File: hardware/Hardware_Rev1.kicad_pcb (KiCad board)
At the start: 2 copper layers, 147.3 x 100.3 mm, 163 parts, among them J1 RJ45_LED_Shielded, J2 6P6C, Q1 BSS138, Q10 AO3401A, Q11 AO3401A, Q12 AO3401A, Q13 BSS138, Q14 BSS138, Q15 BSS138, Q16 AO3401A, Q17 AO3401A, Q18 AO3401A, Q19 BSS138, Q2 BSS138, Q20 BSS138, Q21 BSS138, Q22 AO3401A, Q23 AO3401A, Q24 AO3401A, Q3 BSS138, Q4 AO3401A, Q5 AO3401A, Q6 AO3401A, Q7 BSS138, Q8 BSS138, Q9 BSS138, U1 OKI, U2 Teensy4.1_DEV-16771

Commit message: Fixed mosfet circuits
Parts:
- turned Q10 to -90 degrees
- turned Q11 to -90 degrees
- turned Q12 to -90 degrees
- turned Q16 to -90 degrees
- turned Q17 to -90 degrees
- turned Q18 to -90 degrees
- turned Q22 to -90 degrees
- turned Q23 to -90 degrees
- turned Q24 to -90 degrees
- turned Q4 to -90 degrees
- turned Q5 to -90 degrees
- turned Q6 to -90 degrees
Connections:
- Q10 pad 2: Net-(Conn8-Pad1) -> +12V
- Q10 pad 3: +12V -> Net-(Conn8-Pad1)
- Q11 pad 2: Net-(Conn10-Pad1) -> +12V
- Q11 pad 3: +12V -> Net-(Conn10-Pad1)
- Q12 pad 2: Net-(Conn12-Pad1) -> +12V
- Q12 pad 3: +12V -> Net-(Conn12-Pad1)
- Q16 pad 2: Net-(Conn14-Pad1) -> +12V
- Q16 pad 3: +12V -> Net-(Conn14-Pad1)
- Q17 pad 2: Net-(Conn16-Pad1) -> +12V
- Q17 pad 3: +12V -> Net-(Conn16-Pad1)
- Q18 pad 2: Net-(Conn18-Pad1) -> +12V
- Q18 pad 3: +12V -> Net-(Conn18-Pad1)
- Q22 pad 2: Net-(Conn20-Pad1) -> +12V
- Q22 pad 3: +12V -> Net-(Conn20-Pad1)
- Q23 pad 2: Net-(Conn22-Pad1) -> +12V
- Q23 pad 3: +12V -> Net-(Conn22-Pad1)
- Q24 pad 2: Net-(Conn24-Pad1) -> +12V
- Q24 pad 3: +12V -> Net-(Conn24-Pad1)
- Q4 pad 2: Net-(Conn2-Pad1) -> +12V
- Q4 pad 3: +12V -> Net-(Conn2-Pad1)
- Q5 pad 2: Net-(Conn4-Pad1) -> +12V
- Q5 pad 3: +12V -> Net-(Conn4-Pad1)
- Q6 pad 2: Net-(Conn6-Pad1) -> +12V
- Q6 pad 3: +12V -> Net-(Conn6-Pad1)
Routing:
- net +12V: track 38.9 -> 27.5 mm
- net Net-(Q5-Pad1): track 3.82 -> 12.7 mm, vias 0 -> 2
- net Net-(Q22-Pad1): track 3.76 -> 12.6 mm, vias 0 -> 2
- net Net-(Q16-Pad1): track 3.76 -> 12.6 mm, vias 0 -> 2
- net Net-(Q6-Pad1): track 3.76 -> 12.6 mm, vias 0 -> 2
- net Net-(Q18-Pad1): track 3.76 -> 12.6 mm, vias 0 -> 2
- net Net-(Q12-Pad1): track 3.76 -> 12.6 mm, vias 0 -> 2
- net Net-(Q10-Pad1): track 3.76 -> 12.6 mm, vias 0 -> 2
- net Net-(Q23-Pad1): track 3.78 -> 12.5 mm, vias 0 -> 2
- net Net-(Q24-Pad1): track 3.79 -> 12.5 mm, vias 0 -> 2
- net Net-(Q11-Pad1): track 3.91 -> 12.5 mm, vias 0 -> 2
- net Net-(Q4-Pad1): track 3.77 -> 12.3 mm, vias 0 -> 2
- net Net-(Q17-Pad1): track 3.78 -> 12.3 mm, vias 0 -> 2
- net Heater4: track 35.1 -> 43.3 mm
- net Heater2: track 51.6 -> 59.8 mm
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
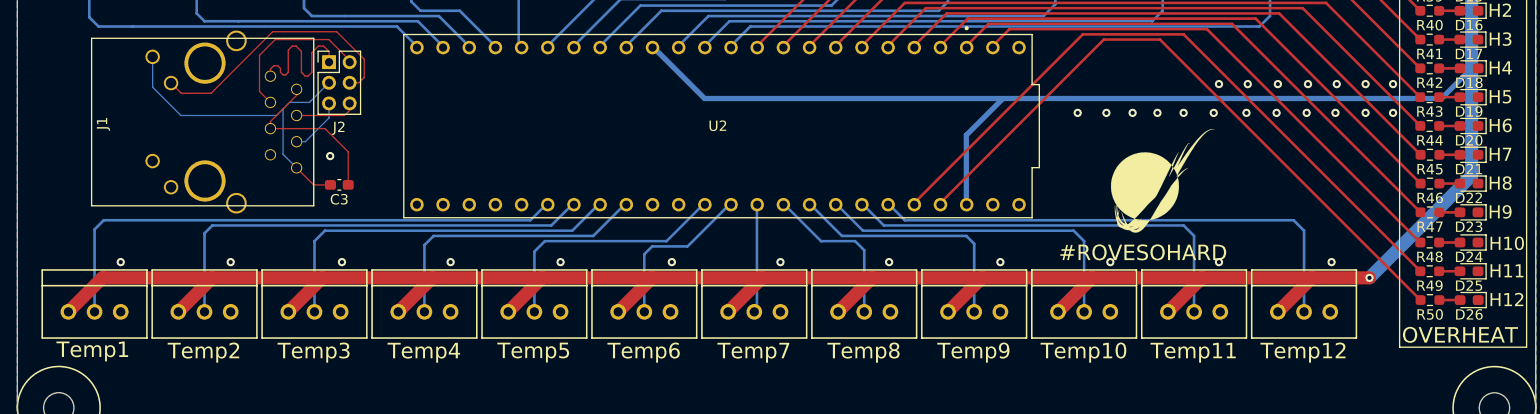
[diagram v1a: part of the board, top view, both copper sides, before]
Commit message: Moved sensor power trace
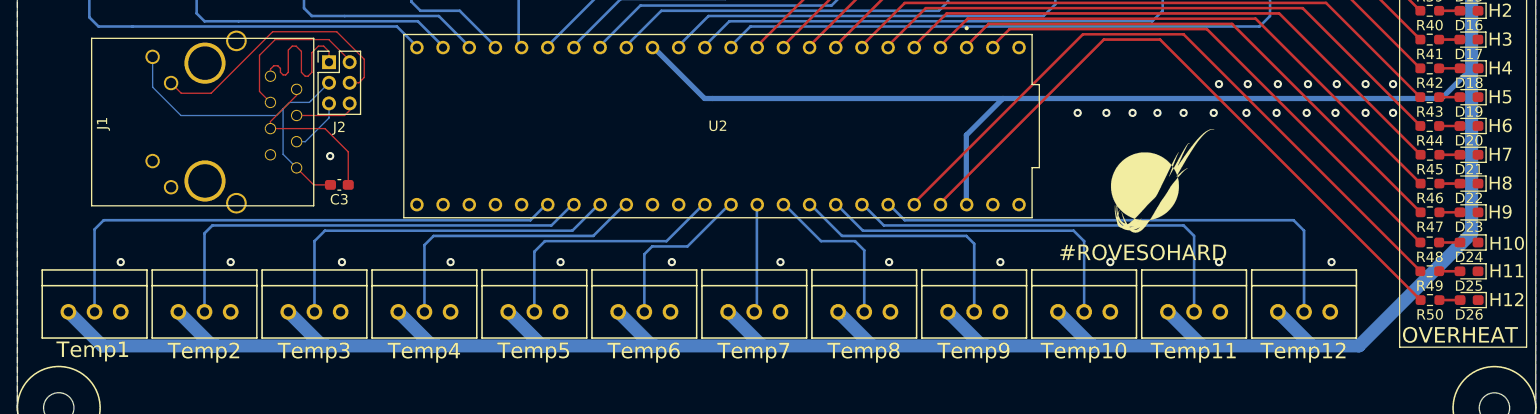
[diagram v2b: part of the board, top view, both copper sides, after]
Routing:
- net +3V3: track 334.6 -> 343.1 mm, vias 1 -> 0
- net GND: vias 71 -> 73
- net (no net): vias 2 -> 0
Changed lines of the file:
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@@
     (style (thickness 0.15) (arrow_length 1.27) (text_position_mode 0) (extension_height 0.58642) (extension_offset 0.5) keep_text_aligned)
   )
-  (via (at 122.936 129.794) (size 0.8) (drill 0.4) (layers "F.Cu" "B.Cu") (free) (net 0))
-  (via (at 112.395 129.794) (size 0.8) (drill 0.4) (layers "F.Cu" "B.Cu") (free) (net 0))
   (segment (start 146.685 83.9705) (end 143.916 83.9705) (width 0.508) (layer "F.Cu") (net 1))
   (segment (start 143.916 83.9705) (end 143.891 83.9955) (width 0.508) (layer "F.Cu") (net 1))
@@
   (via (at 187.96 95.504) (size 0.8) (drill 0.4) (layers "F.Cu" "B.Cu") (free) (net 2))
   (via (at 176.403 129.794) (size 0.8) (drill 0.4) (layers "F.Cu" "B.Cu") (free) (net 2))
+  (via (at 122.936 129.794) (size 0.8) (drill 0.4) (layers "F.Cu" "B.Cu") (free) (net 2))
   (via (at 106.426 79.502) (size 0.8) (drill 0.4) (layers "F.Cu" "B.Cu") (free) (net 2))
   (via (at 101.6 129.794) (size 0.8) (drill 0.4) (layers "F.Cu" "B.Cu") (free) (net 2))
@@
   (via (at 159.512 115.316) (size 0.8) (drill 0.4) (layers "F.Cu" "B.Cu") (free) (net 2))
   (via (at 168.148 115.316) (size 0.8) (drill 0.4) (layers "F.Cu" "B.Cu") (free) (net 2))
+  (via (at 112.395 129.794) (size 0.8) (drill 0.4) (layers "F.Cu" "B.Cu") (free) (net 2))
   (via (at 165.481 129.794) (size 0.8) (drill 0.4) (layers "F.Cu" "B.Cu") (free) (net 2))
   (segment (start 157.074 83.9955) (end 157.099 83.9705) (width 0.635) (layer "F.Cu") (net 3))
@@
   (segment (start 161.95 82.1205) (end 161.925 82.1455) (width 0.508) (layer "F.Cu") (net 4))
   (segment (start 89.0285 82.1205) (end 89.027 82.122) (width 0.508) (layer "F.Cu") (net 4))
-  (segment (start 99.822 131.318) (end 110.49 131.318) (width 1.27) (layer "F.Cu") (net 5))
-  (segment (start 160.528 134.62) (end 163.83 131.318) (width 1.27) (layer "F.Cu") (net 5))
-  (segment (start 153.162 131.318) (end 163.83 131.318) (width 1.27) (layer "F.Cu") (net 5))
-  (segment (start 85.852 134.62) (end 89.154 131.318) (width 1.27) (layer "F.Cu") (net 5))
-  (segment (start 64.516 134.62) (end 67.818 131.318) (width 1.27) (layer "F.Cu") (net 5))
-  (segment (start 163.83 131.318) (end 174.498 131.318) (width 1.27) (layer "F.Cu") (net 5))
-  (segment (start 96.52 134.62) (end 99.822 131.318) (width 1.27) (layer "F.Cu") (net 5))
-  (segment (start 110.49 131.318) (end 121.158 131.318) (width 1.27) (layer "F.Cu") (net 5))
-  (segment (start 128.524 134.62) (end 131.826 131.318) (width 1.27) (layer "F.Cu") (net 5))
-  (segment (start 131.826 131.318) (end 142.494 131.318) (width 1.27) (layer "F.Cu") (net 5))
-  (segment (start 78.486 131.318) (end 89.154 131.318) (width 1.27) (layer "F.Cu") (net 5))
-  (segment (start 142.494 131.318) (end 153.162 131.318) (width 1.27) (layer "F.Cu") (net 5))
-  (segment (start 117.856 134.62) (end 121.158 131.318) (width 1.27) (layer "F.Cu") (net 5))
-  (segment (start 149.86 134.62) (end 153.162 131.318) (width 1.27) (layer "F.Cu") (net 5))
-  (segment (start 107.188 134.62) (end 110.49 131.318) (width 1.27) (layer "F.Cu") (net 5))
-  (segment (start 75.184 134.62) (end 78.486 131.318) (width 1.27) (layer "F.Cu") (net 5))
   (segment (start 189.992 77.6235) (end 190.0185 77.597) (width 1.27) (layer "F.Cu") (net 5))
-  (segment (start 139.192 134.62) (end 142.494 131.318) (width 1.27) (layer "F.Cu") (net 5))
-  (segment (start 171.196 134.62) (end 174.498 131.318) (width 1.27) (layer "F.Cu") (net 5))
-  (segment (start 57.15 131.318) (end 67.818 131.318) (width 1.27) (layer "F.Cu") (net 5))
-  (segment (start 53.848 134.62) (end 57.15 131.318) (width 1.27) (layer "F.Cu") (net 5))
   (segment (start 189.992 80.264) (end 189.992 77.6235) (width 1.27) (layer "F.Cu") (net 5))
-  (segment (start 67.818 131.318) (end 78.486 131.318) (width 1.27) (layer "F.Cu") (net 5))
-  (segment (start 121.158 131.318) (end 131.826 131.318) (width 1.27) (layer "F.Cu") (net 5))
   (segment (start 189.9685 75.438) (end 189.9685 77.547) (width 0.508) (layer "F.Cu") (net 5))
   (segment (start 189.9685 77.547) (end 190.0185 77.597) (width 0.508) (layer "F.Cu") (net 5))
-  (segment (start 89.154 131.318) (end 99.822 131.318) (width 1.27) (layer "F.Cu") (net 5))
-  (segment (start 174.498 131.318) (end 180.086 131.318) (width 1.27) (layer "F.Cu") (net 5))
-  (via (at 180.086 131.318) (size 0.8) (drill 0.4) (layers "F.Cu" "B.Cu") (net 5))
   (segment (start 189.992 80.264) (end 189.992 96.012) (width 1.27) (layer "B.Cu") (net 5))
+  (segment (start 110.744 137.922) (end 121.158 137.922) (width 1.27) (layer "B.Cu") (net 5))
   (segment (start 189.992 110.998) (end 189.992 96.012) (width 1.27) (layer "B.Cu") (net 5))
+  (segment (start 142.494 137.922) (end 142.875 137.922) (width 1.27) (layer "B.Cu") (net 5))
   (segment (start 189.992 96.012) (end 189.992 96.901) (width 1.27) (layer "B.Cu") (net 5))
+  (segment (start 153.289 137.922) (end 163.83 137.922) (width 1.27) (layer "B.Cu") (net 5))
+  (segment (start 78.867 137.922) (end 89.662 137.922) (width 1.27) (layer "B.Cu") (net 5))
+  (segment (start 142.875 137.922) (end 153.289 137.922) (width 1.27) (layer "B.Cu") (net 5))
+  (segment (start 121.158 137.922) (end 131.826 137.922) (width 1.27) (layer "B.Cu") (net 5))
+  (segment (start 160.528 134.62) (end 163.83 137.922) (width 1.27) (layer "B.Cu") (net 5))
+  (segment (start 75.184 134.62) (end 78.486 137.922) (width 1.27) (layer "B.Cu") (net 5))
+  (segment (start 117.856 134.62) (end 121.158 137.922) (width 1.27) (layer "B.Cu") (net 5))
+  (segment (start 189.992 127) (end 189.992 110.998) (width 1.27) (layer "B.Cu") (net 5))
+  (segment (start 68.199 137.922) (end 78.867 137.922) (width 1.27) (layer "B.Cu") (net 5))
   (segment (start 189.738 96.901) (end 189.992 96.901) (width 0.508) (layer "B.Cu") (net 5))
+  (segment (start 179.07 137.922) (end 189.992 127) (width 1.27) (layer "B.Cu") (net 5))
+  (segment (start 171.196 134.62) (end 174.498 137.922) (width 1.27) (layer "B.Cu") (net 5))
+  (segment (start 89.154 137.922) (end 89.662 137.922) (width 1.27) (layer "B.Cu") (net 5))
+  (segment (start 78.486 137.922) (end 78.867 137.922) (width 1.27) (layer "B.Cu") (net 5))
+  (segment (start 67.818 137.922) (end 68.199 137.922) (width 1.27) (layer "B.Cu") (net 5))
   (segment (start 140.97 124.079) (end 140.97 117.475) (width 0.508) (layer "B.Cu") (net 5))
+  (segment (start 107.188 134.62) (end 110.49 137.922) (width 1.27) (layer "B.Cu") (net 5))
   (segment (start 110.49 108.839) (end 115.57 113.919) (width 0.508) (layer "B.Cu") (net 5))
-  (segment (start 189.992 121.412) (end 189.992 110.998) (width 1.27) (layer "B.Cu") (net 5))
+  (segment (start 53.848 134.62) (end 57.15 137.922) (width 1.27) (layer "B.Cu") (net 5))
+  (segment (start 163.83 137.922) (end 174.498 137.922) (width 1.27) (layer "B.Cu") (net 5))
+  (segment (start 100.33 137.922) (end 110.744 137.922) (width 1.27) (layer "B.Cu") (net 5))
+  (segment (start 128.524 134.62) (end 131.826 137.922) (width 1.27) (layer "B.Cu") (net 5))
   (segment (start 187.071 113.919) (end 189.992 110.998) (width 0.508) (layer "B.Cu") (net 5))
+  (segment (start 139.192 134.62) (end 142.494 137.922) (width 1.27) (layer "B.Cu") (net 5))
+  (segment (start 131.826 137.922) (end 142.875 137.922) (width 1.27) (layer "B.Cu") (net 5))
+  (segment (start 149.86 134.62) (end 153.162 137.922) (width 1.27) (layer "B.Cu") (net 5))
   (segment (start 116.332 113.919) (end 144.526 113.919) (width 0.508) (layer "B.Cu") (net 5))
+  (segment (start 110.49 137.922) (end 110.744 137.922) (width 1.27) (layer "B.Cu") (net 5))
   (segment (start 140.97 117.475) (end 144.526 113.919) (width 0.508) (layer "B.Cu") (net 5))
+  (segment (start 89.662 137.922) (end 100.33 137.922) (width 1.27) (layer "B.Cu") (net 5))
+  (segment (start 64.516 134.62) (end 67.818 137.922) (width 1.27) (layer "B.Cu") (net 5))
+  (segment (start 85.852 134.62) (end 89.154 137.922) (width 1.27) (layer "B.Cu") (net 5))
   (segment (start 144.526 113.919) (end 187.071 113.919) (width 0.508) (layer "B.Cu") (net 5))
+  (segment (start 153.162 137.922) (end 153.289 137.922) (width 1.27) (layer "B.Cu") (net 5))
   (segment (start 115.57 113.919) (end 116.332 113.919) (width 0.508) (layer "B.Cu") (net 5))
-  (segment (start 180.086 131.318) (end 189.992 121.412) (width 1.27) (layer "B.Cu") (net 5))
+  (segment (start 57.15 137.922) (end 68.199 137.922) (width 1.27) (layer "B.Cu") (net 5))
+  (segment (start 174.498 137.922) (end 179.07 137.922) (width 1.27) (layer "B.Cu") (net 5))
+  (segment (start 96.52 134.62) (end 99.822 137.922) (width 1.27) (layer "B.Cu") (net 5))
+  (segment (start 99.822 137.922) (end 100.33 137.922) (width 1.27) (layer "B.Cu") (net 5))
   (segment (start 112.6975 83.947) (end 112.649 83.9955) (width 0.508) (layer "F.Cu") (net 6))
   (segment (start 115.3945 83.9955) (end 115.443 83.947) (width 0.508) (layer "F.Cu") (net 6))

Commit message: Started layout heater ports
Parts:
- removed Conn14, Conn15, Conn16, Conn17, Conn18, Conn19, Conn20, Conn21, Conn22, Conn23, Conn24, Conn25: Molex_SL_02, MRDT_Connectors:MOLEX_SL_02_Vertical
- removed G***: LOGO, MRDT_Silkscreens:0_MRDT_Logo_20mm
- removed G***: LOGO, MRDT_Silkscreens:z_sig_Grant_Brinker_30mmx7.3
- removed G***: LOGO, MRDT_Silkscreens:0_MRDT_Logo_10mm
- removed J2: 6P6C, Connector_PinHeader_2.00mm:PinHeader_2x03_P2.00mm_Vertical
- added C4: 100uF, Capacitor_THT:CP_Radial_D6.3mm_P2.50mm, F.Cu at (-76.9, 75.9)
- added C5: 220uF, Capacitor_THT:CP_Radial_D6.3mm_P2.50mm, F.Cu at (-65.6, 65.2)
- added C6: 470uF, Capacitor_THT:CP_Radial_D10.0mm_P2.50mm, F.Cu at (-134.5, 106.6)
- Conn10, Conn11, Conn12, Conn13, Conn2, Conn3, Conn4, Conn5, Conn6, Conn7, Conn8, Conn9: value Molex_SL_02 -> AndersonPP; footprint MRDT_Connectors:MOLEX_SL_02_Vertical -> MRDT_Connectors:Square_Anderson_2_V_Side_By_Side
- Q10, Q11, Q12, Q16, Q17, Q18, Q22, Q23, Q24, Q4, Q5, Q6: value AO3401A -> Q_PMOS_GSD; footprint Package_TO_SOT_SMD:SOT-23 -> Package_TO_SOT_SMD:SOT-23-3
- R10: value 1000 -> 1k
- R20, R39, R40, R41, R42, R43, R44, R45, R46, R47, R48, R49, R50: value 120 -> 100
- U2: footprint MRDT_Shields:Teensy_4_1_Bare -> MRDT_Shields:Teensy_4_1_Ethernet
- moved D22 340.0 mm to (-150.1, 110.9), turned to 0 degrees
- moved D18 335.5 mm to (-145.7, 110.9), turned to 0 degrees
- moved D12 334.0 mm to (-154.5, 110.9), turned to 0 degrees
- moved D23 315.3 mm to (-125.2, 111.0), turned to 0 degrees
- moved U1 308.7 mm to (-122.8, 56.3)
- moved D26 306.9 mm to (-116.5, 112.4), turned to 0 degrees
- moved D15 302.0 mm to (-112.1, 112.4), turned to 0 degrees
- moved Q16 290.6 mm to (-124.9, 107.5), turned to 0 degrees
- moved R10 283.7 mm to (-94.6, 111.4)
- moved D25 283.6 mm to (-91.8, 96.7), turned to 0 degrees
- moved R41 280.1 mm to (-94.1, 103.9), turned to 0 degrees
- moved R46 276.1 mm to (-89.2, 99.2), turned to 0 degrees
- moved R42 275.8 mm to (-89.8, 104.2), turned to 0 degrees
- moved Q22 272.1 mm to (-96.6, 96.0), turned to 0 degrees
- moved D24 270.2 mm to (-76.3, 81.2), turned to 0 degrees
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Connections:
- net Net-(R39-Pad2) renamed Overheat1
- net Net-(R40-Pad2) renamed Overheat2
- net Net-(R41-Pad2) renamed Overheat3
- net Net-(R42-Pad2) renamed Overheat4
- net Net-(R43-Pad2) renamed Overheat5
- net Net-(R44-Pad2) renamed Overheat6
- net Net-(R45-Pad2) renamed Overheat7
- net Net-(R46-Pad2) renamed Overheat8
- net Net-(R47-Pad2) renamed Overheat9
- net Net-(R48-Pad2) renamed Overheat10
- net Net-(R49-Pad2) renamed Overheat11
- net Net-(R50-Pad2) renamed Overheat12
- C3 pad 2: Net-(C3-Pad2) -> GND
- Conn10 pad 1: Net-(Conn10-Pad1) -> GND
- Conn10 pad 2: GND -> /H11
- Conn11 pad 1: Net-(Conn10-Pad1) -> GND
- Conn11 pad 2: GND -> /H4
- Conn12 pad 1: Net-(Conn12-Pad1) -> GND
- Conn12 pad 2: GND -> /H8
- Conn13 pad 1: Net-(Conn12-Pad1) -> GND
- Conn13 pad 2: GND -> /H12
- Conn2 pad 1: Net-(Conn2-Pad1) -> GND
- Conn2 pad 2: GND -> /H1
- Conn3 pad 1: Net-(Conn2-Pad1) -> GND
- Conn3 pad 2: GND -> /H5
- Conn4 pad 1: Net-(Conn4-Pad1) -> GND
- Conn4 pad 2: GND -> /H9
- Conn5 pad 1: Net-(Conn4-Pad1) -> GND
- Conn5 pad 2: GND -> /H2
- Conn6 pad 1: Net-(Conn6-Pad1) -> GND
- Conn6 pad 2: GND -> /H6
- Conn7 pad 1: Net-(Conn6-Pad1) -> GND
- Conn7 pad 2: GND -> /H10
- Conn8 pad 1: Net-(Conn8-Pad1) -> GND
- Conn8 pad 2: GND -> /H3
- Conn9 pad 1: Net-(Conn8-Pad1) -> GND
- Conn9 pad 2: GND -> /H7
- J1 pad 1: /TX+ -> T+
- J1 pad 10: Net-(J1-Pad10) -> LED
- J1 pad 3: /TX- -> T-
- J1 pad 4: /RX+ -> R+
- J1 pad 6: /RX- -> R-
- J1 pad 8: Net-(C3-Pad2) -> GND
- J1 pad 9: Net-(C3-Pad2) -> GND
- Q10 pad 2: +12V -> /H10
- Q10 pad 3: Net-(Conn8-Pad1) -> +12V
- Q11 pad 2: +12V -> /H2
- Q11 pad 3: Net-(Conn10-Pad1) -> +12V
- Q12 pad 2: +12V -> /H6
- Q12 pad 3: Net-(Conn12-Pad1) -> +12V
- Q16 pad 2: +12V -> /H3
- Q16 pad 3: Net-(Conn14-Pad1) -> +12V
- Q17 pad 2: +12V -> /H11
- Q17 pad 3: Net-(Conn16-Pad1) -> +12V
- Q18 pad 2: +12V -> /H7
- Q18 pad 3: Net-(Conn18-Pad1) -> +12V
- Q22 pad 2: +12V -> /H12
- Q22 pad 3: Net-(Conn20-Pad1) -> +12V
- Q23 pad 2: +12V -> /H4
- Q23 pad 3: Net-(Conn22-Pad1) -> +12V
- Q24 pad 2: +12V -> /H8
- Q24 pad 3: Net-(Conn24-Pad1) -> +12V
- Q4 pad 2: +12V -> /H9
- Q4 pad 3: Net-(Conn2-Pad1) -> +12V
- Q5 pad 2: +12V -> /H1
- Q5 pad 3: Net-(Conn4-Pad1) -> +12V
- Q6 pad 2: +12V -> /H5
- Q6 pad 3: Net-(Conn6-Pad1) -> +12V
- R17 pad 2: Net-(Conn8-Pad1) -> /H10
- R18 pad 2: Net-(Conn10-Pad1) -> /H2
- R19 pad 2: Net-(Conn12-Pad1) -> /H6
- R21 pad 2: Net-(Q16-Pad1) -> Net-(Q17-Pad1)
- R22 pad 1: Net-(Q16-Pad1) -> Net-(Q17-Pad1)
- R23 pad 2: Net-(Q17-Pad1) -> Net-(Q16-Pad1)
- R24 pad 1: Net-(Q17-Pad1) -> Net-(Q16-Pad1)
- R27 pad 2: Net-(Conn14-Pad1) -> /H11
- R28 pad 2: Net-(Conn16-Pad1) -> /H3
- R29 pad 2: Net-(Conn18-Pad1) -> /H7
- R36 pad 2: Net-(Conn20-Pad1) -> /H12
- R37 pad 2: Net-(Conn22-Pad1) -> /H4
- R38 pad 2: Net-(Conn24-Pad1) -> /H8
- R7 pad 2: Net-(Conn2-Pad1) -> /H9
- R8 pad 2: Net-(Conn4-Pad1) -> /H1
- R9 pad 2: Net-(Conn6-Pad1) -> /H5
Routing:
- net +3V3: track 343.1 -> 0.00 mm
- net Heater12: track 88.3 -> 0.00 mm, vias 2 -> 0
- net Heater11: track 80.1 -> 0.00 mm, vias 2 -> 0
- net Heater10: track 71.9 -> 0.00 mm, vias 2 -> 0
- net Overheat1: track 66.9 -> 0.00 mm
- net Heater9: track 66.4 -> 0.00 mm, vias 2 -> 0
- net Overheat11: track 65.4 -> 0.00 mm
- net Overheat2: track 65.1 -> 0.00 mm
- net Overheat12: track 63.7 -> 0.00 mm
- net Overheat3: track 63.3 -> 0.00 mm
- net Heater1: track 67.9 -> 5.27 mm, vias 2 -> 1
- net Overheat4: track 61.5 -> 0.00 mm
- net Heater2: track 59.8 -> 0.00 mm, vias 2 -> 0
- net Overheat5: track 59.7 -> 0.00 mm
- net Heater8: track 58.3 -> 0.00 mm, vias 2 -> 0
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- added copper zone on F.Cu, net /H1
- removed copper zone on F.Cu, net Net-(Conn10-Pad1)
- removed copper zone on F.Cu, net Net-(Conn12-Pad1)
- removed copper zone on F.Cu, net Net-(Conn14-Pad1)
- removed copper zone on F.Cu, net Net-(Conn16-Pad1)
- removed copper zone on F.Cu, net Net-(Conn18-Pad1)
- removed copper zone on F.Cu, net Net-(Conn2-Pad1)
- removed copper zone on F.Cu, net Net-(Conn20-Pad1)
- removed copper zone on F.Cu, net Net-(Conn22-Pad1)
- removed copper zone on F.Cu, net Net-(Conn24-Pad1)
- removed copper zone on F.Cu, net Net-(Conn4-Pad1)
- removed copper zone on F.Cu, net Net-(Conn6-Pad1)
- removed copper zone on F.Cu, net Net-(Conn8-Pad1)
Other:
- board size 147.3 x 100.3 mm -> 144.8 x 63.5 mm
- board text removed: "#ROVESOHARD"
- board text removed: "12V"
- board text removed: "3.3V"
- board text removed: "H1"
- board text removed: "H10"
- board text removed: "H11"
- board text removed: "H12"
- board text removed: "H2"
- board text removed: "H3"
- board text removed: "H4"
- board text removed: "H5"
- board text removed: "H6"
- board text removed: "H7"
- board text removed: "H8"
- board text removed: "H9"
- board text removed: "Heater1"
- board text removed: "Heater10"
- board text removed: "Heater11"
- board text removed: "Heater12"
- board text removed: "Heater2"
- board text removed: "Heater3"
- board text removed: "Heater4"
- board text removed: "Heater5"
- board text removed: "Heater6"
- board text removed: "Heater7"
- board text removed: "Heater8"
- board text removed: "Heater9"
- board text removed: "OVERHEAT"
- board text removed: "Science Heater Board, Rev 1 Mars Rover Design Team Missouri S&T 2023 Grant Brinker"
- board text removed: "Temp1"
- board text removed: "Temp10"
- board text removed: "Temp11"
- board text removed: "Temp12"
- board text removed: "Temp2"
- board text removed: "Temp3"
- board text removed: "Temp4"
- board text removed: "Temp5"
- board text removed: "Temp6"
- board text removed: "Temp7"
- board text removed: "Temp8"
- board text removed: "Temp9"

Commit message: Better heater circuit
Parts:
- Q2, R3, R4, R52: moved to B.Cu
- moved C6 219.5 mm to (83.2, 78.5), turned to 180 degrees
- moved C4 161.1 mm to (83.1, 94.7), turned to 180 degrees
- moved C5 150.4 mm to (83.1, 87.6), turned to 180 degrees
- moved R4 7.38 mm to (105.4, 80.0), turned to 0 degrees
- moved R3 4.66 mm to (101.1, 80.0), turned to 0 degrees
- moved Q2 4.46 mm to (105.2, 83.8), turned to 0 degrees
- moved D2 2.17 mm to (105.4, 77.7), turned to 0 degrees
- moved R52 1.93 mm to (101.1, 82.8)
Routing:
- net Net-(Q2-Pad3): track 11.0 -> 3.90 mm, vias 2 -> 0
- net Net-(Q5-Pad1): track 10.7 -> 6.14 mm, vias 2 -> 1
- net Net-(D2-Pad2): track 4.27 -> 3.06 mm
- net +12V: track 2.18 -> 1.44 mm, vias 0 -> 1
- net Heater1: track 5.27 -> 5.29 mm, vias 1 -> 0
